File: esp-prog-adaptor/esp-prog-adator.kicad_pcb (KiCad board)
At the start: 2 copper layers, 40.6 x 55.9 mm, 6 parts, among them J1 Conn_02x19_Odd_Even, J2 Conn_02x19_Odd_Even, J5 Conn_01x03_Male, J6 Conn_01x03_Male

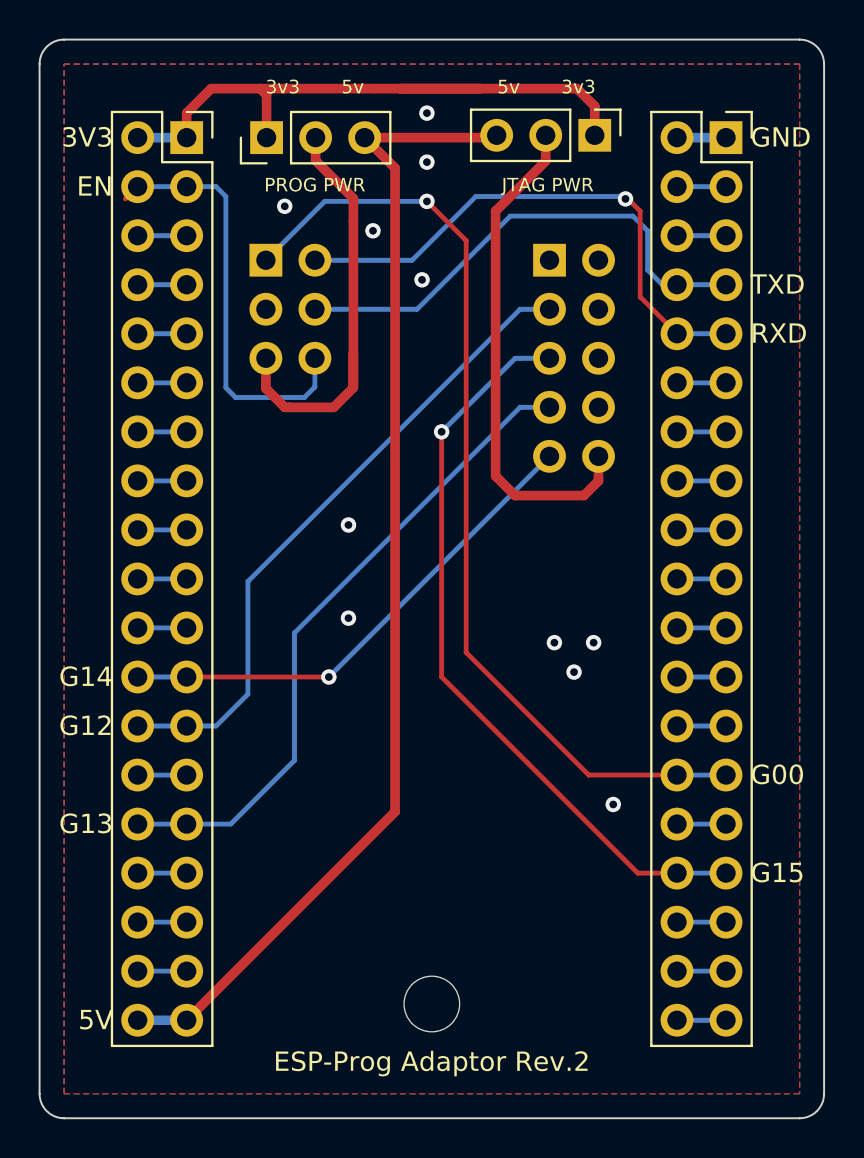
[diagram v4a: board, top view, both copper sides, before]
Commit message: esp_prog_adapter 크기 최적화 (rev 2)
Signed-off-by: Ju, Gyeong-min <jcmh74@gmail.com>
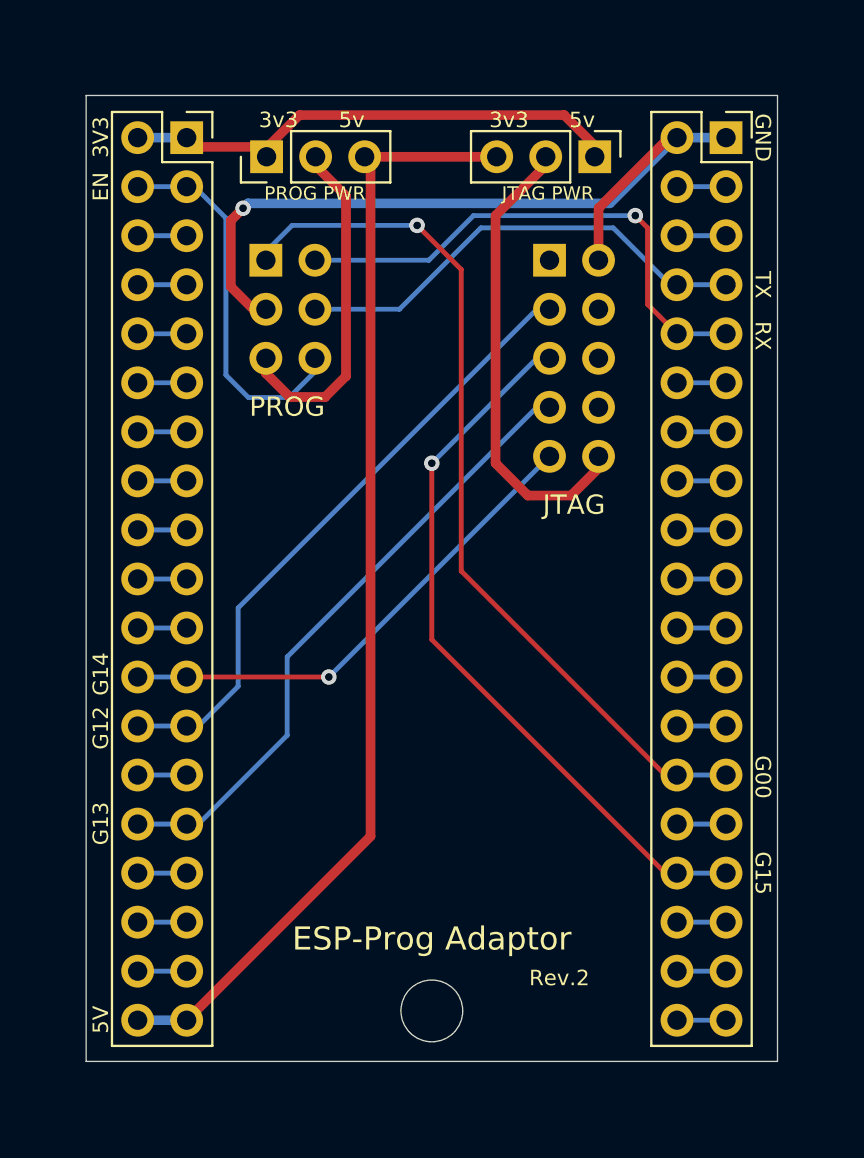
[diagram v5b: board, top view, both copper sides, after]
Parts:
- moved J6 1.11 mm to (166.7, 80.6)
- moved J5 0.99 mm to (149.7, 80.6)
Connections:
- JTAG1 pad 1: (no net) -> unconnected-(JTAG1-Pad1)
- JTAG1 pad 4: (no net) -> unconnected-(JTAG1-Pad4)
- JTAG1 pad 6: (no net) -> unconnected-(JTAG1-Pad6)
- JTAG1 pad 8: (no net) -> unconnected-(JTAG1-Pad8)
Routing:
- net GND: track 2.54 -> 41.4 mm, vias 11 -> 1
- net +3V3: track 45.6 -> 26.5 mm
- net /Vprog: track 22.4 -> 17.9 mm
- net /G00: track 49.9 -> 45.8 mm
- net /EN: track 22.8 -> 19.7 mm
- net +5V: track 60.3 -> 58.2 mm
- net /Vjtag: track 26.1 -> 24.2 mm
- net /TXD: track 26.0 -> 24.3 mm
- net /TCK(G13): track 34.1 -> 32.7 mm
- net /RXD: track 28.2 -> 27.1 mm
- net /TDO(G15): track 38.8 -> 37.7 mm
- net /TDI(G12): track 33.7 -> 32.7 mm
- removed copper zone on B.Cu, net GND
- removed copper zone on F.Cu, net GND
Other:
- board size 40.6 x 55.9 mm -> 35.8 x 50 mm
- board text added: "ESP-Prog Adaptor"
- board text added: "JTAG"
- board text added: "PROG"
- board text added: "RX"
- board text added: "Rev.2"
- board text added: "TX"
- board text removed: "5v 3v3"
- board text removed: "ESP-Prog Adaptor Rev.2"
- board text removed: "RXD"
- board text removed: "TXD"

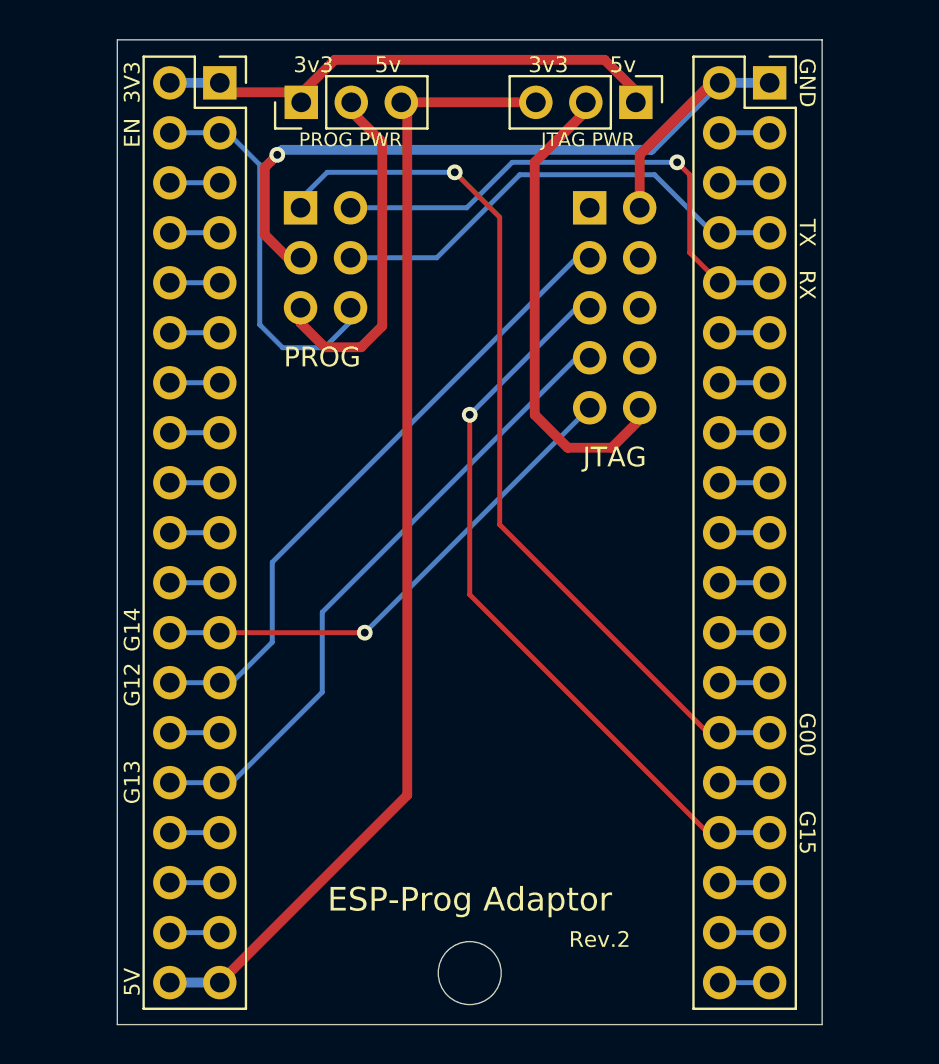
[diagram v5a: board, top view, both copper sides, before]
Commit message: esp_prog_adaptor에 나사홀 추가
Signed-off-by: Ju, Gyeong-min <jcmh74@gmail.com>
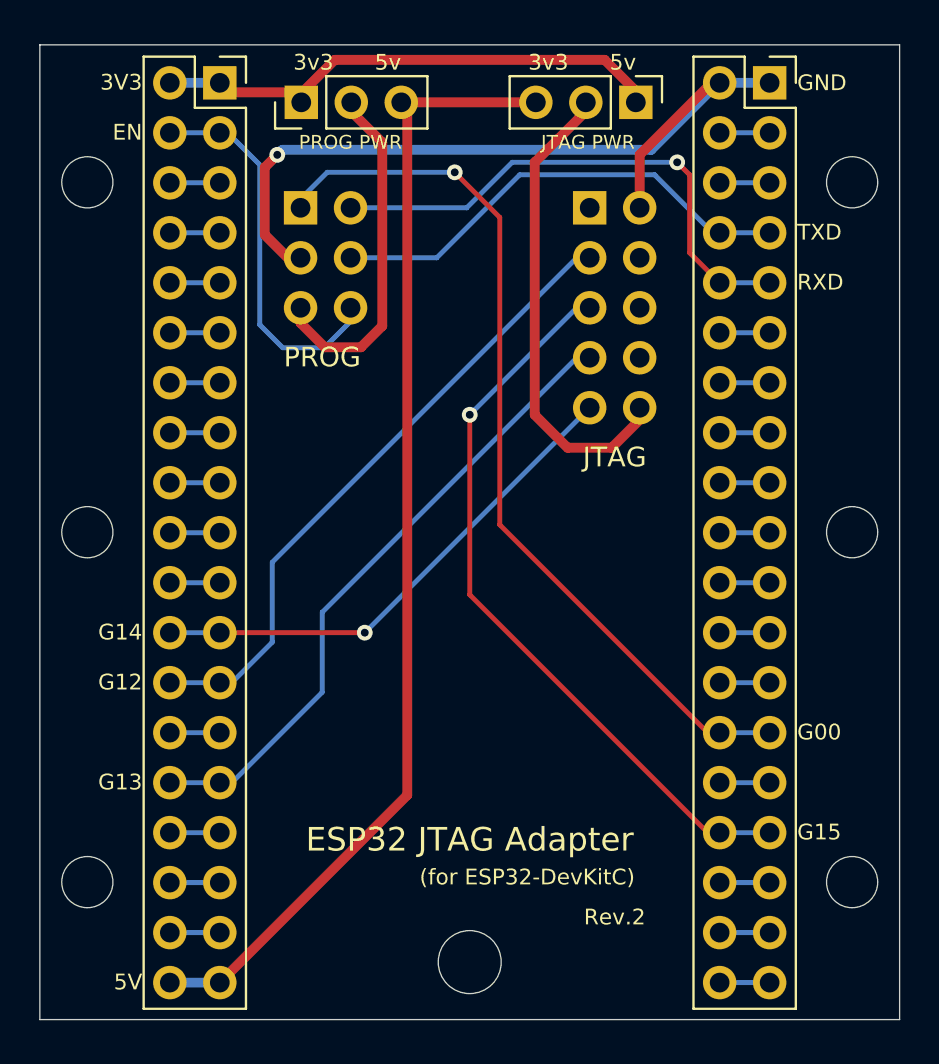
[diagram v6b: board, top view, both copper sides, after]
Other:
- board size 35.8 x 50 mm -> 43.7 x 49.5 mm
- board text added: "(for ESP32-DevKitC)"
- board text added: "ESP32 JTAG Adapter"
- board text added: "RXD"
- board text added: "TXD"
- board text removed: "ESP-Prog Adaptor"
- board text removed: "RX"
- board text removed: "TX"
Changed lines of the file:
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@@
   (paper "A4")
   (title_block
-    (title "ESP32 JTAG Adapter")
+    (title "ESP32 JTAG Adapter (for ESP32-DevKitC)")
     (date "2021-09-02")
     (rev "2")
@@
   (setup
     (pad_to_mask_clearance 0)
-    (aux_axis_origin 140.335 127.508)
+    (aux_axis_origin 136.398 127.254)
     (pcbplotparams
       (layerselection 0x00010f0_ffffffff)
@@
     )
   )
-  (gr_circle (center 158.242 124.892) (end 159.842 124.892) (layer "Edge.Cuts") (width 0.05) (fill none))
-  (gr_rect (start 140.335 77.47) (end 176.149 127.508) (layer "Edge.Cuts") (width 0.05) (fill none))
+  (gr_circle (center 158.242 124.333) (end 159.842 124.333) (layer "Edge.Cuts") (width 0.05) (fill none))
+  (gr_circle (center 138.811 102.489) (end 140.111 102.489) (layer "Edge.Cuts") (width 0.05) (fill none))
+  (gr_rect (start 136.398 77.724) (end 180.086 127.254) (layer "Edge.Cuts") (width 0.05) (fill none))
+  (gr_circle (center 138.811 84.709) (end 140.111 84.709) (layer "Edge.Cuts") (width 0.05) (fill none))
+  (gr_circle (center 177.673 120.269) (end 178.973 120.269) (layer "Edge.Cuts") (width 0.05) (fill none))
+  (gr_circle (center 177.673 102.489) (end 178.973 102.489) (layer "Edge.Cuts") (width 0.05) (fill none))
+  (gr_circle (center 177.673 84.709) (end 178.973 84.709) (layer "Edge.Cuts") (width 0.05) (fill none))
+  (gr_circle (center 138.811 120.269) (end 140.111 120.269) (layer "Edge.Cuts") (width 0.05) (fill none))
   (gr_text "PROG" (at 150.749 93.599) (layer "B.SilkS")
     (effects (font (size 1 1) (thickness 0.15)) (justify mirror))
@@
     (effects (font (size 1 1) (thickness 0.15)) (justify mirror))
   )
-  (gr_text "5V" (at 141.097 125.349 90) (layer "F.SilkS")
+  (gr_text "5V" (at 141.605 125.349) (layer "F.SilkS")
+    (effects (font (size 0.8 0.8) (thickness 0.15)) (justify right))
+  )
+  (gr_text "EN" (at 141.605 82.169) (layer "F.SilkS")
+    (effects (font (size 0.8 0.8) (thickness 0.15)) (justify right))
+  )
+  (gr_text "G15" (at 174.879 117.729) (layer "F.SilkS")
+    (effects (font (size 0.8 0.8) (thickness 0.15)) (justify left))
+  )
+  (gr_text "3v3      5v" (at 152.019 78.613) (layer "F.SilkS")
     (effects (font (size 0.8 0.8) (thickness 0.15)))
   )
-  (gr_text "EN" (at 141.097 82.1944 90) (layer "F.SilkS")
-    (effects (font (size 0.8 0.8) (thickness 0.15)))
-  )
-  (gr_text "G15" (at 175.387 117.7544 270) (layer "F.SilkS")
-    (effects (font (size 0.8 0.8) (thickness 0.15)))
-  )
-  (gr_text "3v3      5v" (at 152.019 78.74) (layer "F.SilkS")
-    (effects (font (size 0.8 0.8) (thickness 0.15)))
-  )
-  (gr_text "JTAG PWR" (at 164.247 82.55) (layer "F.SilkS")
+  (gr_text "JTAG PWR" (at 164.247 82.677) (layer "F.SilkS")
     (effects (font (size 0.7 0.7) (thickness 0.1)))
   )
-  (gr_text "G12" (at 141.097 110.236 90) (layer "F.SilkS")
-    (effects (font (size 0.8 0.8) (thickness 0.15)))
-  )
-  (gr_text "TX" (at 175.387 87.2744 270) (layer "F.SilkS")
-    (effects (font (size 0.8 0.8) (thickness 0.15)))
+  (gr_text "G12" (at 141.605 110.109) (layer "F.SilkS")
+    (effects (font (size 0.8 0.8) (thickness 0.15)) (justify right))
+  )
+  (gr_text "TXD" (at 174.879 87.249) (layer "F.SilkS")
+    (effects (font (size 0.8 0.8) (thickness 0.15)) (justify left))
   )
   (gr_text "PROG" (at 150.749 93.599) (layer "F.SilkS")
@@
     (effects (font (size 1 1) (thickness 0.15)))
   )
-  (gr_text "ESP-Prog Adaptor" (at 158.242 121.158) (layer "F.SilkS")
+  (gr_text "ESP32 JTAG Adapter\n" (at 158.242 118.11) (layer "F.SilkS")
     (effects (font (size 1.2 1.2) (thickness 0.15)))
   )
-  (gr_text "PROG PWR" (at 152.182 82.55) (layer "F.SilkS")
+  (gr_text "(for ESP32-DevKitC)" (at 161.163 120.015) (layer "F.SilkS")
+    (effects (font (size 0.8 0.8) (thickness 0.15)))
+  )
+  (gr_text "PROG PWR" (at 152.182 82.677) (layer "F.SilkS")
     (effects (font (size 0.7 0.7) (thickness 0.1)))
   )
-  (gr_text "G13" (at 141.097 115.189 90) (layer "F.SilkS")
+  (gr_text "G13" (at 141.605 115.189) (layer "F.SilkS")
+    (effects (font (size 0.8 0.8) (thickness 0.15)) (justify right))
+  )
+  (gr_text "G14" (at 141.605 107.569) (layer "F.SilkS")
+    (effects (font (size 0.8 0.8) (thickness 0.15)) (justify right))
+  )
+  (gr_text "RXD" (at 174.879 89.789) (layer "F.SilkS")
+    (effects (font (size 0.8 0.8) (thickness 0.15)) (justify left))
+  )
+  (gr_text "Rev.2" (at 165.608 122.047) (layer "F.SilkS")
     (effects (font (size 0.8 0.8) (thickness 0.15)))
   )
-  (gr_text "G14" (at 141.097 107.442 90) (layer "F.SilkS")
+  (gr_text "3V3" (at 141.605 79.629) (layer "F.SilkS")
+    (effects (font (size 0.8 0.8) (thickness 0.15)) (justify right))
+  )
+  (gr_text "G00" (at 174.879 112.649) (layer "F.SilkS")
+    (effects (font (size 0.8 0.8) (thickness 0.15)) (justify left))
+  )
+  (gr_text "3v3      5v" (at 163.957 78.613) (layer "F.SilkS")
     (effects (font (size 0.8 0.8) (thickness 0.15)))
   )
-  (gr_text "RX" (at 175.387 89.916 270) (layer "F.SilkS")
-    (effects (font (size 0.8 0.8) (thickness 0.15)))
-  )
-  (gr_text "Rev.2" (at 164.846 123.19) (layer "F.SilkS")
-    (effects (font (size 0.8 0.8) (thickness 0.15)))
-  )
-  (gr_text "3V3" (at 141.097 79.629 90) (layer "F.SilkS")
-    (effects (font (size 0.8 0.8) (thickness 0.15)))
-  )
-  (gr_text "G00" (at 175.387 112.776 270) (layer "F.SilkS")
-    (effects (font (size 0.8 0.8) (thickness 0.15)))
-  )
-  (gr_text "3v3      5v" (at 163.957 78.74) (layer "F.SilkS")
-    (effects (font (size 0.8 0.8) (thickness 0.15)))
-  )
-  (gr_text "GND" (at 175.387 79.6544 270) (layer "F.SilkS")
-    (effects (font (size 0.8 0.8) (thickness 0.15)))
+  (gr_text "GND" (at 174.879 79.6544) (layer "F.SilkS")
+    (effects (font (size 0.8 0.8) (thickness 0.15)) (justify left))
   )
   (segment (start 148.463 83.312) (end 147.828 83.947) (width 0.5) (layer "F.Cu") (net 1))
